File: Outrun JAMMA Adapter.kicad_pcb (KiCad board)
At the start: 2 copper layers, 111 x 77.8 mm, 31 parts, among them U1 LM386, U2 MCP4902, U3 328P

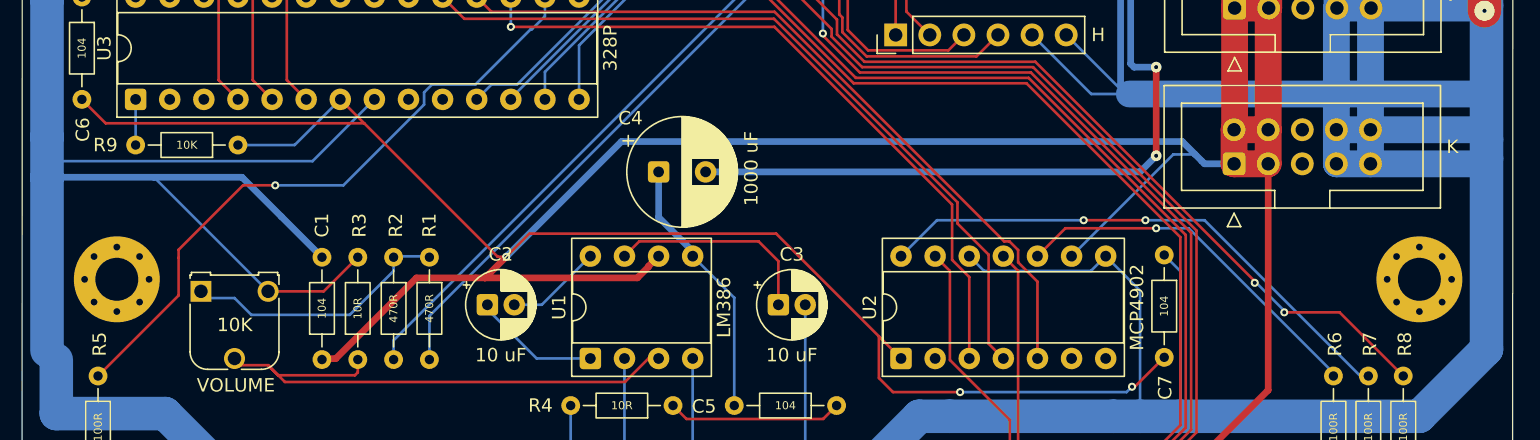
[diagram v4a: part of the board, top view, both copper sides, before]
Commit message: minor trace cleanup
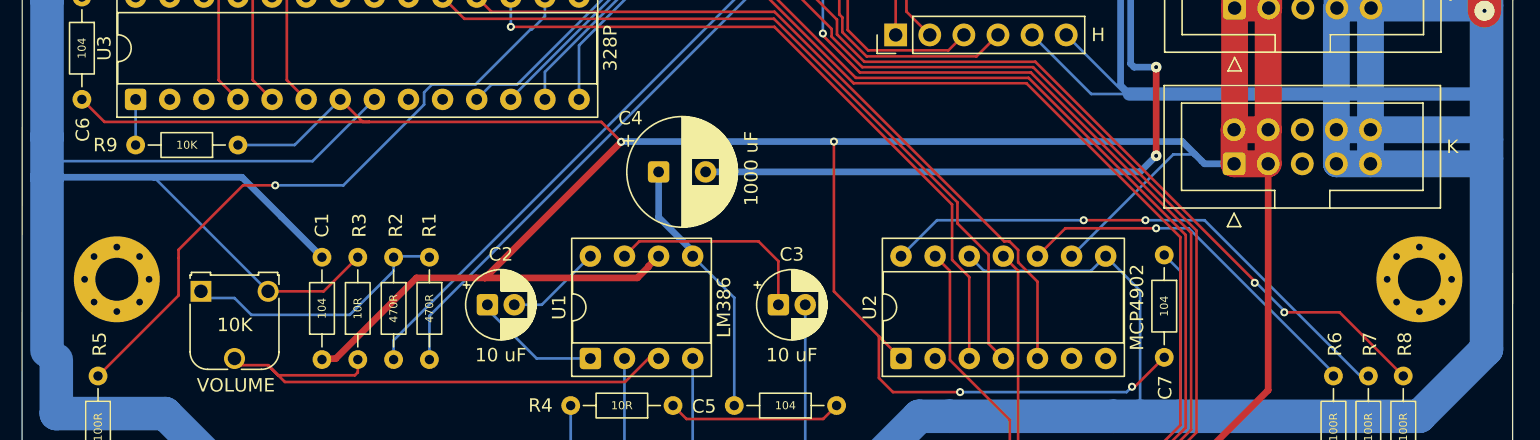
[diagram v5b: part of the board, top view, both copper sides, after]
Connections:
- U3 pad 10: PB7 -> (no net)
- U3 pad 9: PB6 -> (no net)
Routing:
- net +5V: track 359.0 -> 360.9 mm, vias 5 -> 6
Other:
- board text added: "PCB Design Copyright © 2026, Jonathan Zdziarski All Rights Reserved"
- board text removed: "PCB Design Copyright © 2025, Jonathan Zdziarski All Rights Reserved"
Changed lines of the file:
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@@
 			(layers "*.Cu" "*.Mask")
 			(remove_unused_layers no)
-			(net "PB6")
 		)
 		(pad "10" thru_hole circle
@@
 			(layers "*.Cu" "*.Mask")
 			(remove_unused_layers no)
-			(net "PB7")
 		)
 		(pad "11" thru_hole circle
@@
 		)
 	)
-	(gr_text "PCB Design Copyright © 2025, Jonathan Zdziarski\nAll Rights Reserved"
+	(gr_text "PCB Design Copyright © 2026, Jonathan Zdziarski\nAll Rights Reserved"
 		(at 95 91.5 270)
 		(layer "F.Fab")
@@
 		(start 184.2 95)
 		(end 176.4 95)
-		(width 2)
+		(width 1)
 		(layer "B.Cu")
 		(net "GND")
@@
 		(start 184.2 95)
 		(end 186.8 95)
-		(width 2)
+		(width 1)
 		(layer "B.Cu")
 		(net "GND")
@@
 		(start 187 95)
 		(end 202.25 95)
-		(width 2)
+		(width 1)
 		(layer "B.Cu")
 		(net "GND")
@@
 	)
 	(segment
-		(start 117.64 95.4)
-		(end 119.42 97.18)
-		(width 0.2)
+		(start 140.594851 107.865555)
+		(end 139.764851 108.695555)
+		(width 0.5)
 		(layer "F.Cu")
 		(net "+5V")
 	)
 	(segment
-		(start 140.594851 107.865555)
-		(end 139.764851 108.695555)
-		(width 0.5)
+		(start 119.32 97.08)
+		(end 119.8 97.08)
+		(width 0.2)
 		(layer "F.Cu")
 		(net "+5V")
@@
 	)
 	(segment
-		(start 159.4 114.695555)
+		(start 157.952222 113.247778)
 		(end 157.752222 113.047778)
 		(width 0.2)
@@
 	)
 	(segment
-		(start 131.720704 105.4)
-		(end 130 107.120704)
+		(start 159.4 114.695555)
+		(end 157.952222 113.247778)
+		(width 0.2)
+		(layer "F.Cu")
+		(net "+5V")
+	)
+	(segment
+		(start 137.08 97.08)
+		(end 138.560352 98.560352)
 		(width 0.2)
 		(layer "F.Cu")
@@
 	)
 	(segment
-		(start 140.594851 107.825555)
-		(end 140.594851 107.865555)
-		(width 0.5)
+		(start 130 107.120704)
+		(end 138.560352 98.560352)
+		(width 0.2)
 		(layer "F.Cu")
 		(net "+5V")
 	)
 	(segment
-		(start 150.104445 105.4)
-		(end 131.720704 105.4)
-		(width 0.2)
+		(start 140.594851 107.825555)
+		(end 140.594851 107.865555)
+		(width 0.5)
 		(layer "F.Cu")
 		(net "+5V")
@@
 	)
 	(segment
+		(start 100.08 97.08)
+		(end 98.4 95.4)
+		(width 0.2)
+		(layer "F.Cu")
+		(net "+5V")
+	)
+	(segment
 		(start 158.8 117.2)
 		(end 163.8 117.2)
@@
 	)
 	(segment
+		(start 119.8 97.08)
+		(end 100.08 97.08)
+		(width 0.2)
+		(layer "F.Cu")
+		(net "+5V")
+	)
+	(segment
 		(start 117.300078 114.70778)
 		(end 116.2777 114.70778)
@@
 	)
 	(segment
-		(start 128.425149 108.695555)
-		(end 130 107.120704)
-		(width 0.5)
-		(layer "F.Cu")
-		(net "+5V")
-	)
-	(segment
 		(start 195.033352 69.245852)
 		(end 195.03 69.2425)
@@
 	)
 	(segment
-		(start 186.74 97.66)
-		(end 186.74 88.64)
-		(width 2)
-		(layer "F.Cu")
-		(net "+5V")
-	)
-	(segment
-		(start 119.42 97.18)
-		(end 100.17 97.18)
+		(start 117.64 95.4)
+		(end 119.32 97.08)
 		(width 0.2)
 		(layer "F.Cu")
@@
 	)
 	(segment
-		(start 100.17 97.18)
-		(end 98.4 95.41)
-		(width 0.2)
+		(start 186.74 97.66)
+		(end 186.74 88.64)
+		(width 2)
 		(layer "F.Cu")
 		(net "+5V")
@@
 	)
 	(segment
-		(start 119.42 97.18)
-		(end 129.360704 107.120704)
-		(width 0.2)
-		(layer "F.Cu")
-		(net "+5V")
-	)
-	(segment
 		(start 195.033352 75.840122)
 		(end 195.033352 69.245852)
@@
 	)
 	(segment
-		(start 128.4 108.695555)
-		(end 128.425149 108.695555)
-		(width 0.5)
-		(layer "F.Cu")
-		(net "+5V")
-	)
-	(segment
 		(start 186.78 86.06)
 		(end 186.78 83.52)
@@
 	)
 	(segment
-		(start 129.360704 107.120704)
-		(end 130 107.120704)
+		(start 154.4 109.695556)
+		(end 154.4 98.6)
 		(width 0.2)
 		(layer "F.Cu")
@@
 	)
 	(segment
+		(start 128.4 108.695555)
+		(end 128.425149 108.695555)
+		(width 0.5)
+		(layer "F.Cu")
+		(net "+5V")
+	)
+	(segment
 		(start 184.2 97.66)
 		(end 186.74 97.66)
@@
 	)
 	(segment
-		(start 157.752222 113.047778)
-		(end 150.104445 105.4)
-		(width 0.2)
+		(start 128.425149 108.695555)
+		(end 138.560352 98.560352)
+		(width 0.5)
 		(layer "F.Cu")
 		(net "+5V")
@@
 	)
 	(segment
+		(start 119.8 97.08)
+		(end 137.08 97.08)
+		(width 0.2)
+		(layer "F.Cu")
+		(net "+5V")
+	)
+	(segment
 		(start 186.78 88.6)
 		(end 184.24 88.6)
@@
 		(net "+5V")
 	)
+	(segment
+		(start 157.952222 113.247778)
+		(end 154.4 109.695556)
+		(width 0.2)
+		(layer "F.Cu")
+		(net "+5V")
+	)
 	(via
 		(at 194.976319 75.638753)
@@
 	)
 	(via
-		(at 130 107.120704)
+		(at 138.560352 98.560352)
 		(size 0.6)
 		(drill 0.3)
@@
 		(net "+5V")
 	)
+	(via
+		(at 154.4 98.54)
+		(size 0.6)
+		(drill 0.3)
+		(layers "F.Cu" "B.Cu")
+		(net "+5V")
+	)
 	(segment
 		(start 114.24 98.8)
@@
 	)
 	(segment
+		(start 138.580704 98.54)
+		(end 138.560352 98.560352)
+		(width 0.5)
+		(layer "B.Cu")
+		(net "+5V")
+	)
+	(segment
 		(start 176.2 117.2)
 		(end 176.6 116.8)
@@
 	(segment
 		(start 180.343122 98.54)
-		(end 138.580704 98.54)
+		(end 154.4 98.54)
 		(width 0.5)
 		(layer "B.Cu")
@@
 	)
 	(segment
-		(start 138.580704 98.54)
-		(end 130 107.120704)
-		(width 0.5)
-		(layer "B.Cu")
-		(net "+5V")
-	)
-	(segment
 		(start 181.801561 99.998439)
 		(end 182.003122 100.2)
@@
 	)
 	(segment
+		(start 154.4 98.54)
+		(end 138.580704 98.54)
+		(width 0.5)
+		(layer "B.Cu")
+		(net "+5V")
+	)
+	(segment
 		(start 167.3 69.2425)
 		(end 167.3 72.3)
@@
 	)
 	(segment
-		(start 161.94 107.075555)
-		(end 163.04 108.175555)
-		(width 0.2)
-		(layer "F.Cu")
-		(net "REFA")
-	)
-	(segment
-		(start 163.04 114.81119)
-		(end 167.502451 119.273641)
-		(width 0.2)
-		(layer "F.Cu")
-		(net "REFA")
-	)
-	(segment
-		(start 167.502451 119.273641)
-		(end 167.502451 122.502451)
-		(width 0.2)
-		(layer "F.Cu")
-		(net "REFA")
-	)
-	(segment
-		(start 167.502451 122.502451)
-		(end 168 123)
-		(width 0.2)
-		(layer "F.Cu")
-		(net "REFA")
-	)
-	(segment
-		(start 163.04 108.175555)
-		(end 163.04 114.81119)
-		(width 0.2)
-		(layer "F.Cu")
-		(net "REFA")
-	)
-	(via
-		(at 168 123)
-		(size 0.6)
-		(drill 0.3)
-		(layers "F.Cu" "B.Cu")
-		(net "REFA")
-	)
-	(segment
-		(start 174.4 128.8)
-		(end 168.6 123)
-		(width 0.2)
-		(layer "B.Cu")
-		(net "REFA")
-	)
-	(segment
-		(start 168.6 123)
-		(end 168 123)
-		(width 0.2)
-		(layer "B.Cu")
-		(net "REFA")
-	)
-	(segment
-		(start 174.78 128.8)
-		(end 174.4 128.8)
-		(width 0.2)
-		(layer "B.Cu")
-		(net "REFA")
-	)
-	(segment
 		(start 168.65 122.730761)
 		(end 168.65 124.05)
@@
 	)
 	(segment
-		(start 178.92 127.2)
-		(end 177.32 128.8)
+		(start 161.94 107.075555)
+		(end 163.04 108.175555)
 		(width 0.2)
 		(layer "F.Cu")
-		(net "ACCEL")
+		(net "REFA")
 	)
 	(segment
-		(start 190.62 127.2)
-		(end 178.92 127.2)
+		(start 163.04 114.81119)
+		(end 167.502451 119.273641)
 		(width 0.2)
 		(layer "F.Cu")
-		(net "ACCEL")
+		(net "REFA")
 	)
 	(segment
-		(start 194.2 123.62)
-		(end 190.62 127.2)
+		(start 167.502451 119.273641)
+		(end 167.502451 122.502451)
 		(width 0.2)
 		(layer "F.Cu")
-		(net "ACCEL")
+		(net "REFA")
+	)
+	(segment
+		(start 167.502451 122.502451)
+		(end 168 123)
+		(width 0.2)
+		(layer "F.Cu")
+		(net "REFA")
+	)
+	(segment
+		(start 163.04 108.175555)
+		(end 163.04 114.81119)
+		(width 0.2)
+		(layer "F.Cu")
+		(net "REFA")
+	)
+	(via
+		(at 168 123)
+		(size 0.6)
+		(drill 0.3)
+		(layers "F.Cu" "B.Cu")
+		(net "REFA")
+	)
+	(segment
+		(start 174.4 128.8)
+		(end 168.6 123)
+		(width 0.2)
+		(layer "B.Cu")
+		(net "REFA")
+	)
+	(segment
+		(start 168.6 123)
+		(end 168 123)
+		(width 0.2)
+		(layer "B.Cu")
+		(net "REFA")
+	)
+	(segment
+		(start 174.78 128.8)
+		(end 174.4 128.8)
+		(width 0.2)
+		(layer "B.Cu")
+		(net "REFA")
 	)
 	(segment
@@
 	)
 	(segment
+		(start 178.92 127.2)
+		(end 177.32 128.8)
+		(width 0.2)
+		(layer "F.Cu")
+		(net "ACCEL")
+	)
+	(segment
+		(start 190.62 127.2)
+		(end 178.92 127.2)
+		(width 0.2)
+		(layer "F.Cu")
+		(net "ACCEL")
+	)
+	(segment
+		(start 194.2 123.62)
+		(end 190.62 127.2)
+		(width 0.2)
+		(layer "F.Cu")
+		(net "ACCEL")
+	)
+	(segment
